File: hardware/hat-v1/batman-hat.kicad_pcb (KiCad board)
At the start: 4 copper layers, 65 x 56.5 mm, 196 parts, among them J1 BATT pads, J2 Pi 40-pin (female, 11 mm stac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, J3 mPCIe 5.2H, J4 U.FL, J5 Tag-Connect TC2050, J6 PANEL BTN, Q1 CSD19537Q3, Q10 BSS138, Q2 BSS138, Q3 CSD17578Q3A, Q4 CSD17578Q3A, Q5 CSD17578Q3A, Q6 BSS138, Q7 BSS138, Q8 BSS138, Q9 BSS138, SW1 on-board PWR, U1 TPS26631RGER, U10 CAT24C32WI-GT3, U11 SLB9672XU2.0, U12 ATECC608C-TFLXTLS, U13 RV-3028-C7, U14 MAX-M10S-00B, U2 INA226AIDGSR, U3 LMR33640DDDAR, U4 LM74700QDBVRQ1, U5 LM74700QDBVRQ1, U6 LM74700QDBVRQ1, U7 TPS62933FDRLR, U8 INA226AIDGSR, U9 LTC2955ITS8-2#TRPBF

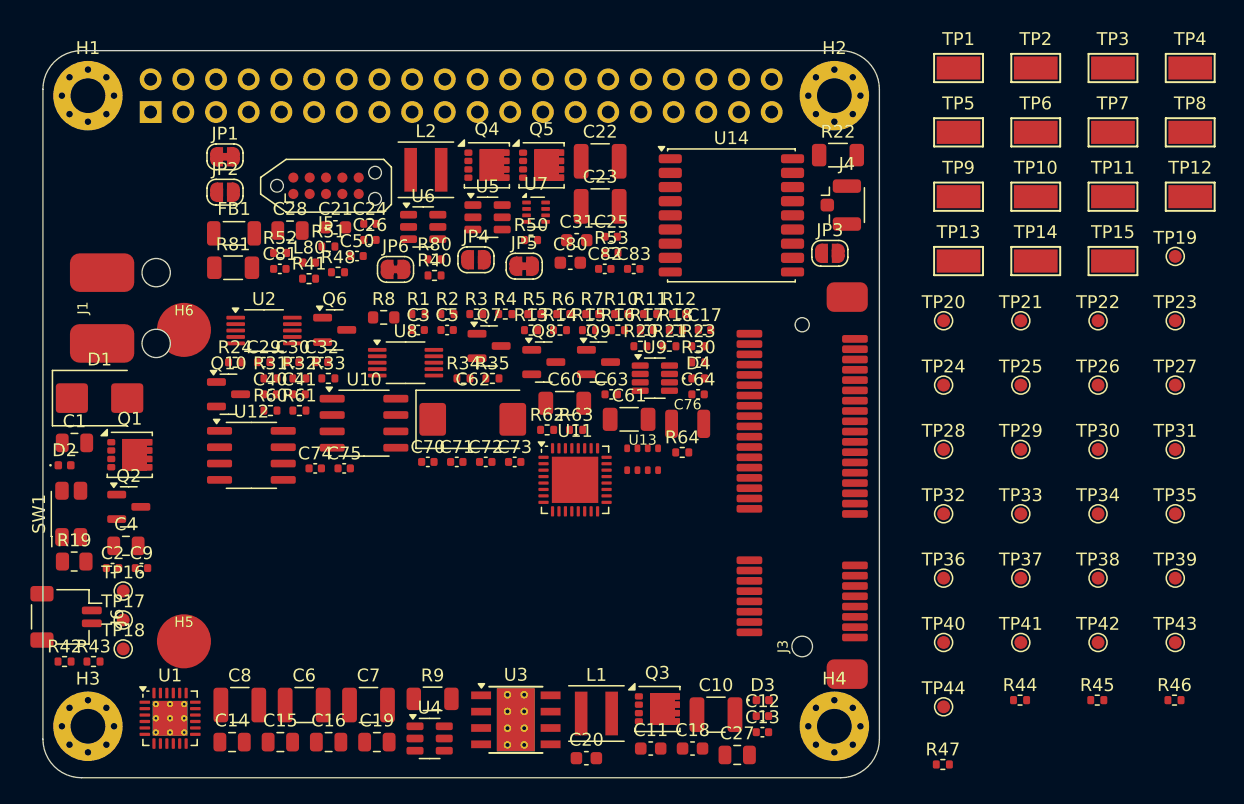
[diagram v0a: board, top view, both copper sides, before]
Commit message: HAT v1: reduce test points (clip pads only for VBAT/5V/3V3 HaLow/GND), re-place
Signals on the 40-pin header are probed on its solder joints; checker
verifies that list. Floorplan: all functional parts and the 4 clip pads
fit; 23 small probe pads still need a home.

Co-Authored-By: Claude Opus 5.5 <noreply@anthropic.com>
Claude-Session: https://claude.ai/code/session_01MLRuxTEmuMV82xcNLE62jW
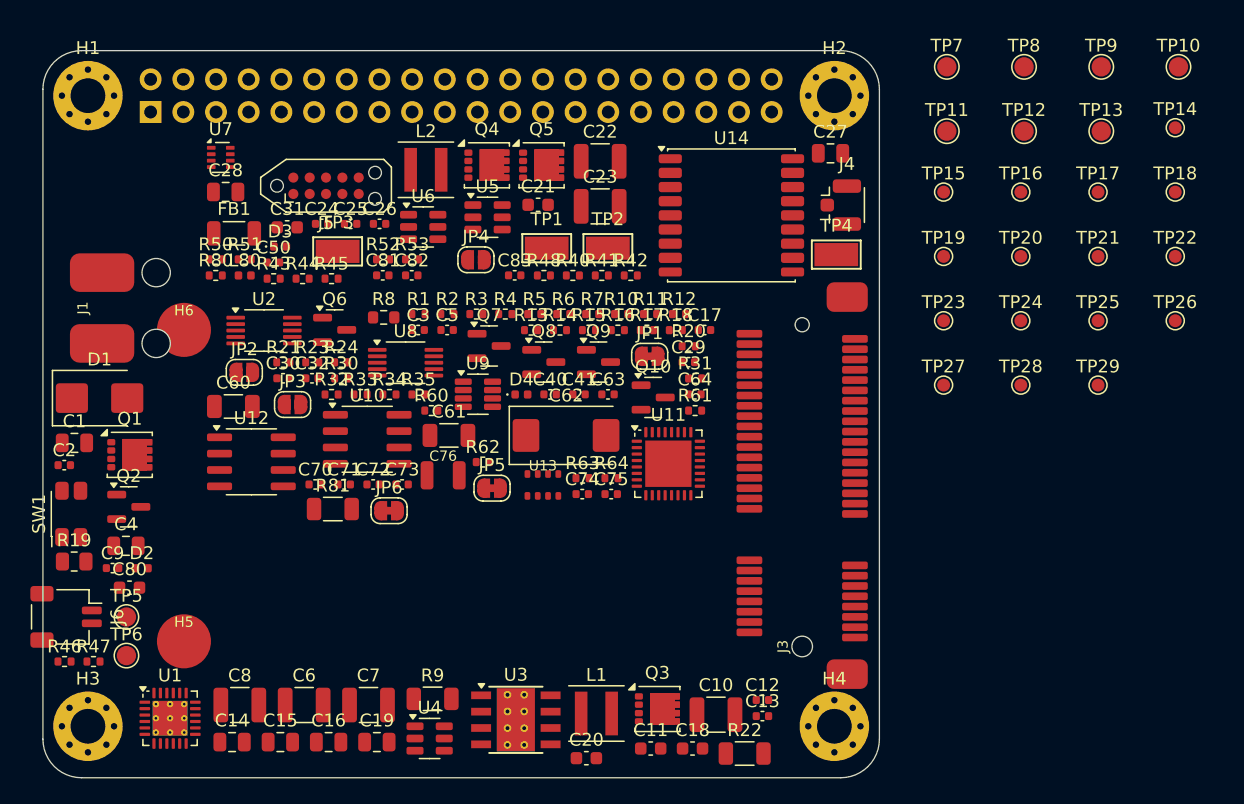
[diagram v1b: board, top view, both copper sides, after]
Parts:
- removed TP30: EN_5V, TestPoint_Pad_D1.0mm
- removed TP31: EN_3V3, TestPoint_Pad_D1.0mm
- removed TP32: PG_5V, TestPoint_Pad_D1.0mm
- removed TP33: BAT_PRESENT_N, TestPoint_Pad_D1.0mm
- removed TP34: EF_FLT_N, TestPoint_Pad_D1.0mm
- removed TP35: EF_SHDN, TestPoint_Pad_D1.0mm
- removed TP36: INA_ALERT_N, TestPoint_Pad_D1.0mm
- removed TP37: RTC_CLKOUT, TestPoint_Pad_D1.0mm
- removed TP38: RTC_INT_N, TestPoint_Pad_D1.0mm
- removed TP39: HALOW_RESET_N, TestPoint_Pad_D1.0mm
- removed TP40: HALOW_WAKE, TestPoint_Pad_D1.0mm
- removed TP41: K1+ (R9), TestPoint_Pad_D1.0mm
- removed TP42: K1- (R9), TestPoint_Pad_D1.0mm
- removed TP43: K2+ (R22), TestPoint_Pad_D1.0mm
- removed TP44: K2- (R22), TestPoint_Pad_D1.0mm
- TP10: value 3V3_GNSS 3.2-3.4 -> 3V3_SEC 3.2-3.4; footprint TestPoint_Keystone_5015_Micro-Minature -> TestPoint_Pad_D1.5mm
- TP11: value VRTC 0-3.3 -> 3V3_GNSS 3.2-3.4; footprint TestPoint_Keystone_5015_Micro-Minature -> TestPoint_Pad_D1.5mm
- TP12: value GND -> VRTC 0-3.3; footprint TestPoint_Keystone_5015_Micro-Minature -> TestPoint_Pad_D1.5mm
- TP13: footprint TestPoint_Keystone_5015_Micro-Minature -> TestPoint_Pad_D1.5mm
- TP14: value GND -> GNSS_RST_N; footprint TestPoint_Keystone_5015_Micro-Minature -> TestPoint_Pad_D1.0mm
- TP15: value GND -> GNSS_SAFEBOOT_N; footprint TestPoint_Keystone_5015_Micro-Minature -> TestPoint_Pad_D1.0mm
- TP16: value I2C1_SDA -> PWR_BTN_N
- TP17: value I2C1_SCL -> LTC_KILL_N
- TP18: value ID_SD -> LTC_ENB
- TP19: value ID_SC -> EN_5V
- TP2: value VSYS 6-17V -> 5V 5.10-5.25
- TP20: value UART5_TX -> EN_3V3
- TP21: value UART5_RX -> PG_5V
- TP22: value GNSS_PPS -> EF_FLT_N
- TP23: value GNSS_RST_N -> EF_SHDN
- TP24: value GNSS_SAFEBOOT_N -> RTC_CLKOUT
- TP25: value PWR_BTN_N -> RTC_INT_N
- TP26: value PWR_INT_N -> K1+ (R9)
- TP27: value LTC_KILL_N -> K1- (R9)
- TP28: value KILL_REQ -> K2+ (R22)
- TP29: value LTC_ENB -> K2- (R22)
- TP3: value 5V 5.10-5.25 -> 3V3 HaLow 3.2-3.4
- TP4: value 5V_PI 5.0-5.2 -> GND
- TP5: value OR 5-17V -> VSYS 6-17V; footprint TestPoint_Keystone_5015_Micro-Minature -> TestPoint_Pad_D1.5mm
- TP6: value 3V3 3.25-3.40 -> 5V_PI 5.0-5.2; footprint TestPoint_Keystone_5015_Micro-Minature -> TestPoint_Pad_D1.5mm
- TP7: value 3V3_MPCIE 3.2-3.4 -> OR 5-17V; footprint TestPoint_Keystone_5015_Micro-Minature -> TestPoint_Pad_D1.5mm
- TP8: value 3V3_PI 3.2-3.4 -> 3V3_BUCK 3.25-3.40; footprint TestPoint_Keystone_5015_Micro-Minature -> TestPoint_Pad_D1.5mm
- TP9: value 3V3_SEC 3.2-3.4 -> 3V3_PI 3.2-3.4; footprint TestPoint_Keystone_5015_Micro-Minature -> TestPoint_Pad_D1.5mm
- moved TP18 89.1 mm to (188.0, 111.0)
- moved R46 86.3 mm to (101.7, 147.5)
- moved TP17 82.7 mm to (182.0, 111.0)
- moved TP6 81.5 mm to (106.5, 147.0)
- moved TP16 76.3 mm to (176.0, 111.0)
- moved TP5 74.8 mm to (106.5, 144.0)
- moved R45 67.9 mm to (122.4, 117.7)
- moved R47 66.5 mm to (103.9, 147.5)
- moved R44 64.7 mm to (120.2, 117.7)
- moved TP3 61.9 mm to (122.9, 115.6)
- moved R42 53.3 mm to (145.7, 117.5)
- moved D3 51.5 mm to (118.4, 115.2)
- moved C27 47.3 mm to (161.2, 108.0)
- moved R22 47.1 mm to (154.5, 154.6)
- moved JP3 43.4 mm to (119.4, 127.5)
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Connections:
- TP10 pad 1: 3V3_GNSS -> 3V3_SEC
- TP11 pad 1: VRTC -> 3V3_GNSS
- TP12 pad 1: GND -> VRTC
- TP14 pad 1: GND -> GNSS_RST_N
- TP15 pad 1: GND -> GNSS_SAFEBOOT_N
- TP16 pad 1: I2C1_SDA -> PWR_BTN_N
- TP17 pad 1: I2C1_SCL -> LTC_KILL_N
- TP18 pad 1: ID_SD -> LTC_ENB
- TP19 pad 1: ID_SC -> EN_5V
- TP2 pad 1: VSYS -> 5V_BUCK
- TP20 pad 1: UART5_TX -> EN_3V3
- TP21 pad 1: UART5_RX -> PG_5V
- TP22 pad 1: GNSS_PPS -> EF_FLT_N
- TP23 pad 1: GNSS_RST_N -> EF_SHDN
- TP24 pad 1: GNSS_SAFEBOOT_N -> RTC_CLKOUT
- TP25 pad 1: PWR_BTN_N -> RTC_INT_N
- TP26 pad 1: PWR_INT_N -> EF_OUT
- TP27 pad 1: LTC_KILL_N -> VSYS
- TP28 pad 1: KILL_REQ -> 3V3_BUCK
- TP29 pad 1: LTC_ENB -> 3V3_SH
- TP3 pad 1: 5V_BUCK -> 3V3_MPCIE
- TP4 pad 1: 5V_PI -> GND
- TP5 pad 1: OR_NODE -> VSYS
- TP6 pad 1: 3V3_BUCK -> 5V_PI
- TP7 pad 1: 3V3_MPCIE -> OR_NODE
- TP8 pad 1: 3V3_PI -> 3V3_BUCK
- TP9 pad 1: 3V3_SEC -> 3V3_PI
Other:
- board text added: "DID NOT FIT (23)"
- board text removed: "DID NOT FIT (45)"

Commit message: HAT v1: probe pads on the back side (user decision); everything placed
Co-Authored-By: Claude Opus 5.5 <noreply@anthropic.com>
Claude-Session: https://claude.ai/code/session_01MLRuxTEmuMV82xcNLE62jW
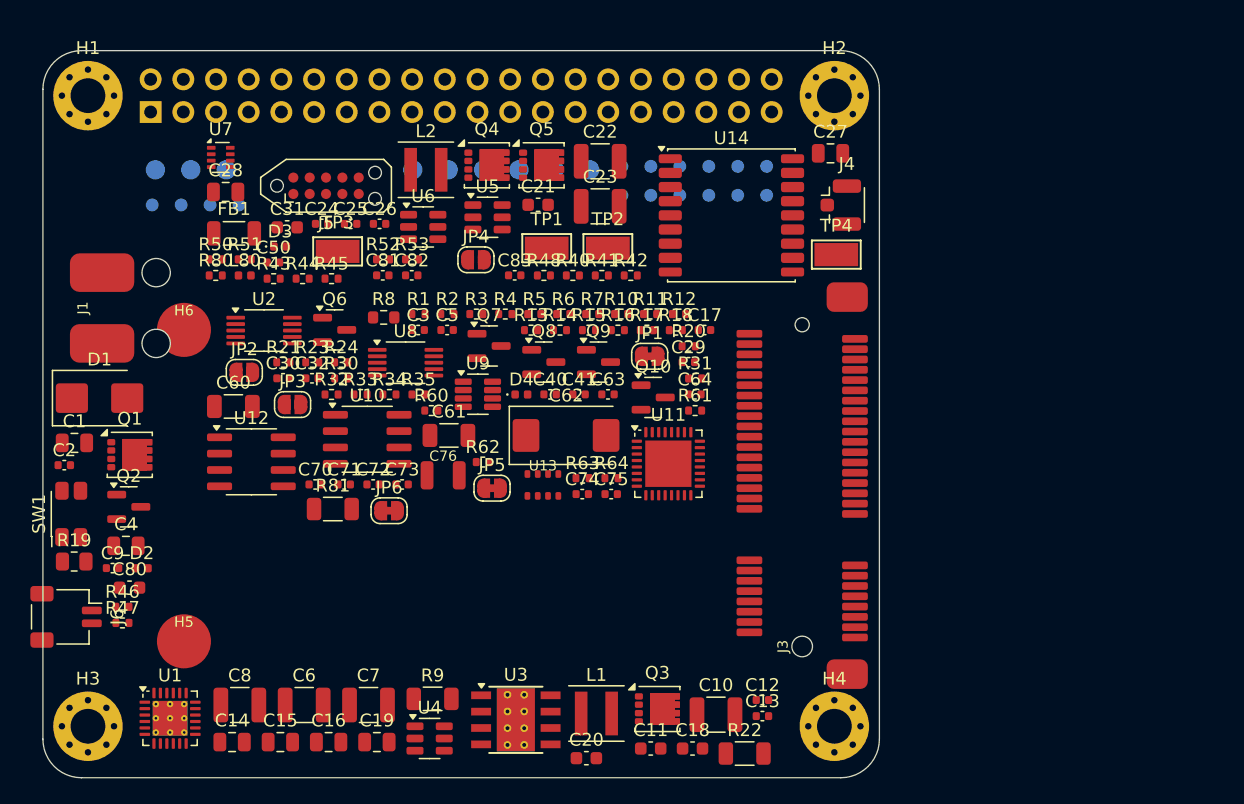
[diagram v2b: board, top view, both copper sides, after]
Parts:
- TP10, TP11, TP12, TP13, TP14, TP15, TP16, TP17, TP18, TP19, TP20, TP21, TP22, TP23, TP24, TP25, TP26, TP27, TP28, TP29, TP5, TP6, TP7, TP8, TP9: moved to B.Cu
- moved TP26 80.0 mm to (108.5, 112.0)
- moved TP29 68.2 mm to (115.2, 112.0)
- moved TP28 64.5 mm to (113.0, 112.0)
- moved TP27 60.9 mm to (110.7, 112.0)
- moved TP7 56.6 mm to (114.2, 109.3)
- moved TP10 54.6 mm to (134.2, 109.3)
- moved TP9 51.4 mm to (131.5, 109.3)
- moved TP8 48.2 mm to (128.7, 109.3)
- moved TP14 43.1 mm to (145.0, 109.0)
- moved TP13 39.9 mm to (142.5, 109.3)
- moved TP22 38.8 mm to (149.5, 111.2)
- moved TP6 38.1 mm to (111.5, 109.3)
- moved TP12 36.6 mm to (139.7, 109.3)
- moved TP21 35.1 mm to (147.2, 111.2)
- moved TP5 34.8 mm to (108.7, 109.3)
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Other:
- board text removed: "DID NOT FIT (23)"

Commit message: HAT v1 floorplan: buck cores on the bottom edge, probe pads on the board edges
Co-Authored-By: Claude Opus 5.5 <noreply@anthropic.com>
Claude-Session: https://claude.ai/code/session_01MLRuxTEmuMV82xcNLE62jW
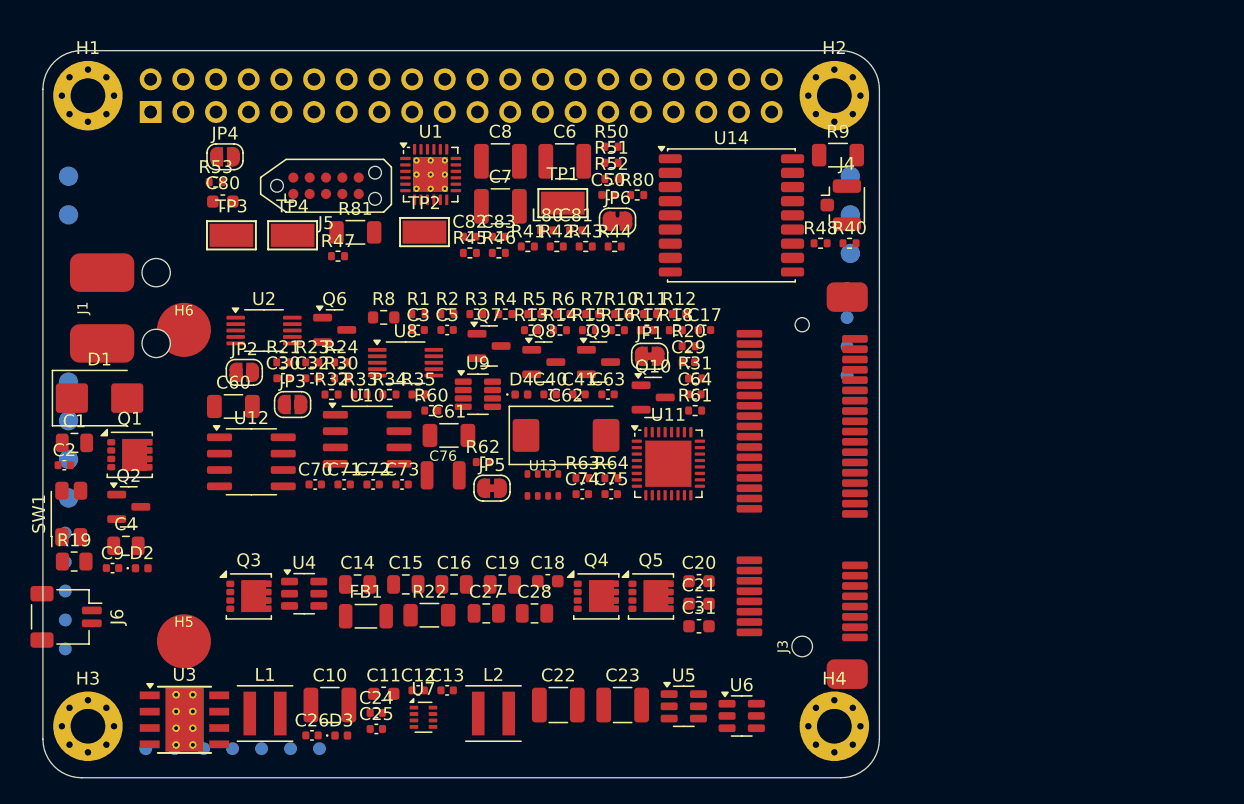
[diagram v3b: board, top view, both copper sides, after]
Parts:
- moved TP19 64.9 mm to (101.7, 144.2)
- moved TP18 61.8 mm to (101.7, 142.0)
- moved TP17 58.7 mm to (101.7, 139.7)
- moved TP22 58.2 mm to (110.2, 154.2)
- moved TP23 58.2 mm to (112.5, 154.2)
- moved TP21 57.6 mm to (101.7, 146.5)
- moved TP20 56.7 mm to (108.0, 154.2)
- moved TP16 55.6 mm to (101.7, 137.5)
- moved R9 52.7 mm to (161.8, 108.1)
- moved TP13 47.9 mm to (102.0, 134.8)
- moved C6 46.9 mm to (140.5, 108.6)
- moved C8 46.9 mm to (135.5, 108.6)
- moved U1 46.9 mm to (130.1, 109.6)
- moved U7 46.3 mm to (129.6, 151.8)
- moved U6 45.3 mm to (154.3, 151.7)
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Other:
- board text added: "under_edge (<=1.9 mm tall)"

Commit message: HAT v1: RV-3028 per Application Manual (land pattern, EVI, VBACKUP 100n, LSM, CLKOUT note)
Co-Authored-By: Claude Opus 5.5 <noreply@anthropic.com>
Claude-Session: https://claude.ai/code/session_01MLRuxTEmuMV82xcNLE62jW
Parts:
- added C33: 10u 50V X7R, C_1210_3225Metric, F.Cu at (124.3, 114.6)
- added C77: 100n 16V, C_0402_1005Metric, F.Cu at (121.2, 135.0)
- R19: value 1R -> 0.47R
- R81: value 47R -> 68R
- moved R40 29.5 mm to (133.2, 115.7)
- moved R45 29.5 mm to (162.7, 116.2)
- moved C82 27.3 mm to (160.4, 115.0)
- moved C83 27.3 mm to (162.7, 115.0)
- moved R46 22.0 mm to (113.4, 116.5)
- moved R81 16.3 mm to (140.5, 114.6)
- moved R48 16.3 mm to (144.2, 115.2)
- moved R44 16.0 mm to (160.4, 116.2)
- moved R42 12.0 mm to (127.9, 116.2)
- moved R43 12.0 mm to (130.2, 116.2)
- moved R47 7.27 mm to (115.7, 116.5)
- moved C81 6.02 mm to (135.4, 114.5)
- moved L80 6.02 mm to (133.2, 114.5)
- moved JP5 4.00 mm to (138.9, 134.0)
- moved U13 3.76 mm to (135.1, 134.0)
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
